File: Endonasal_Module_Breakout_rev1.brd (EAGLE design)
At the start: 80 x 100 mm, 43 parts, among them M0_LIMIT_XOR XOR-SOT353, M3_LIMIT_XOR XOR-SOT353

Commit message: All traces routed
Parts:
- removed M0_LEDG, M1_LEDG, M2_LEDG, M3_LEDG, M4_LEDG, M5_LEDG: (no value), Cannula_1_0:LED-0805
- removed R2, R3, R4, R5, R6: 220, Cannula_1_0:0603-RES
- added POWER_LEDG: (no value), Cannula_1_0:LED-0805
- moved C7 15.2 mm to (43.8, 56.5)
- moved R13 12.1 mm to (43.8, 60.1), turned to 90 degrees
- moved R1 11.4 mm to (5.08, 39.1), turned to 180 degrees
- moved C9 4.13 mm to (30.5, 60.6)
- moved M3_LIMIT_XOR 4.13 mm to (28.2, 60.7)
- moved C5 3.05 mm to (32.0, 36.6)
- moved R11 2.54 mm to (32.0, 33.0)
- moved R17 2.36 mm to (56.1, 35.4)
- moved R19 1.08 mm to (55.4, 18.1), turned to 180 degrees
- moved R18 0.34 mm to (56.0, 25.7), turned to 270 degrees
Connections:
- removed net N$1: M5_LEDG.A, R6.1
- removed net N$2: M4_LEDG.A, R5.1
- removed net N$3: M3_LEDG.A, R4.1
- removed net N$4: M2_LEDG.A, R3.1
- removed net N$5: M1_LEDG.A, R2.1
- net GND: now also POWER_LEDG.C; no longer M0_LEDG.C, M1_LEDG.C, M2_LEDG.C, M3_LEDG.C, M4_LEDG.C, M5_LEDG.C
- net M0_VHALL: now also R1.2
- net M2_VHALL: no longer R1.2, R2.2, R3.2
- net M3_VHALL: no longer R4.2
- net M4_VHALL: no longer R5.2
- net M5_HALL1: now also R19.2; no longer R19.1
- net M5_HALL2: now also R19.1; no longer R19.2
- net M5_VHALL: no longer R6.2
- net N$6: now also POWER_LEDG.A; no longer M0_LEDG.A
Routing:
- net M2A: track 5.08 -> 181.9 mm
- net M2B: track 5.08 -> 174.6 mm
- net M2C: track 5.08 -> 167.3 mm
- net M1A: track 7.18 -> 152.0 mm
- net M1B: track 7.18 -> 146.8 mm
- net M1C: track 7.18 -> 141.8 mm
- net M0A: track 5.08 -> 115.4 mm
- net M0B: track 5.08 -> 108.8 mm
- net M0C: track 5.08 -> 98.1 mm
- net 3.3V_IN: track 30.8 -> 111.8 mm
- net M0_VHALL: track 38.6 -> 84.5 mm
- net M3_VHALL: track 2.21 -> 46.9 mm
- net M4_VHALL: track 0.00 -> 43.2 mm
- net M3_HALL2: track 0.00 -> 40.2 mm
- net M3_HALL3: track 0.00 -> 38.4 mm
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
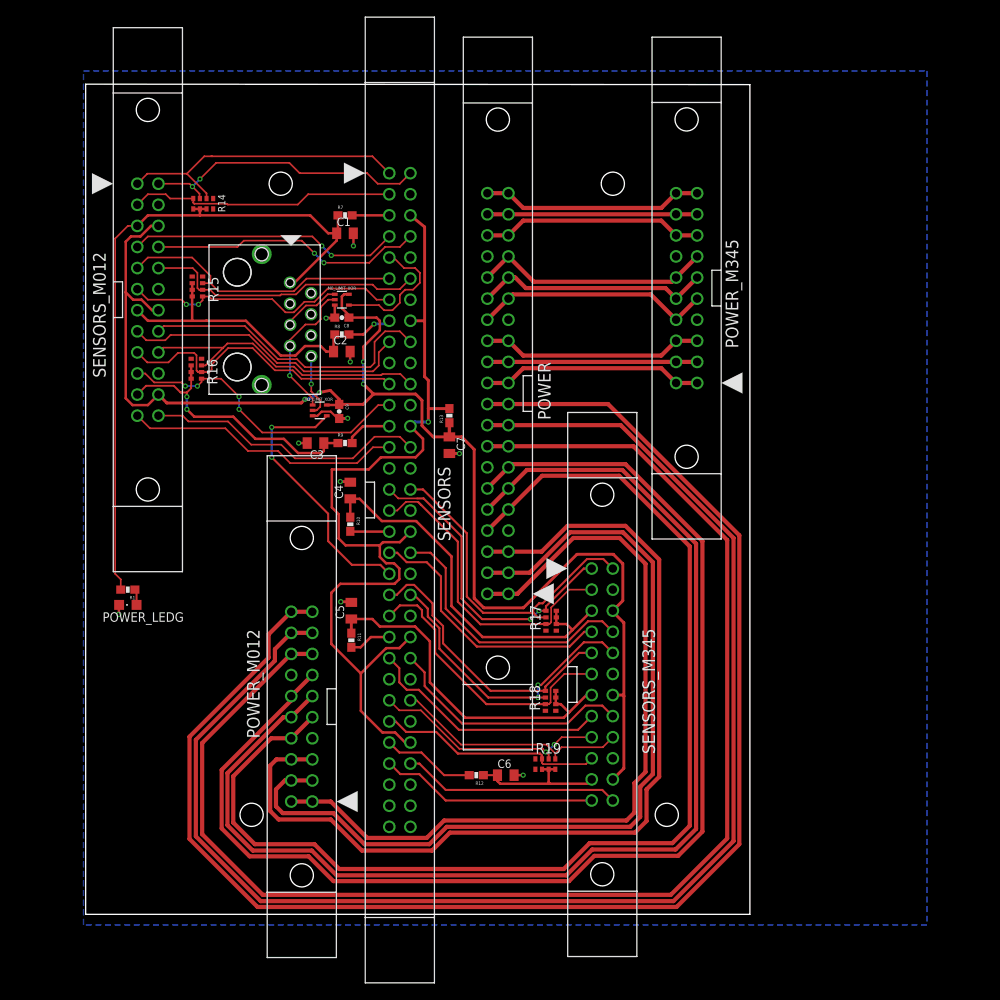
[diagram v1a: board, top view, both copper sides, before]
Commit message: Increased connector spacing
Increased spacing between connectors to be at least 5mm
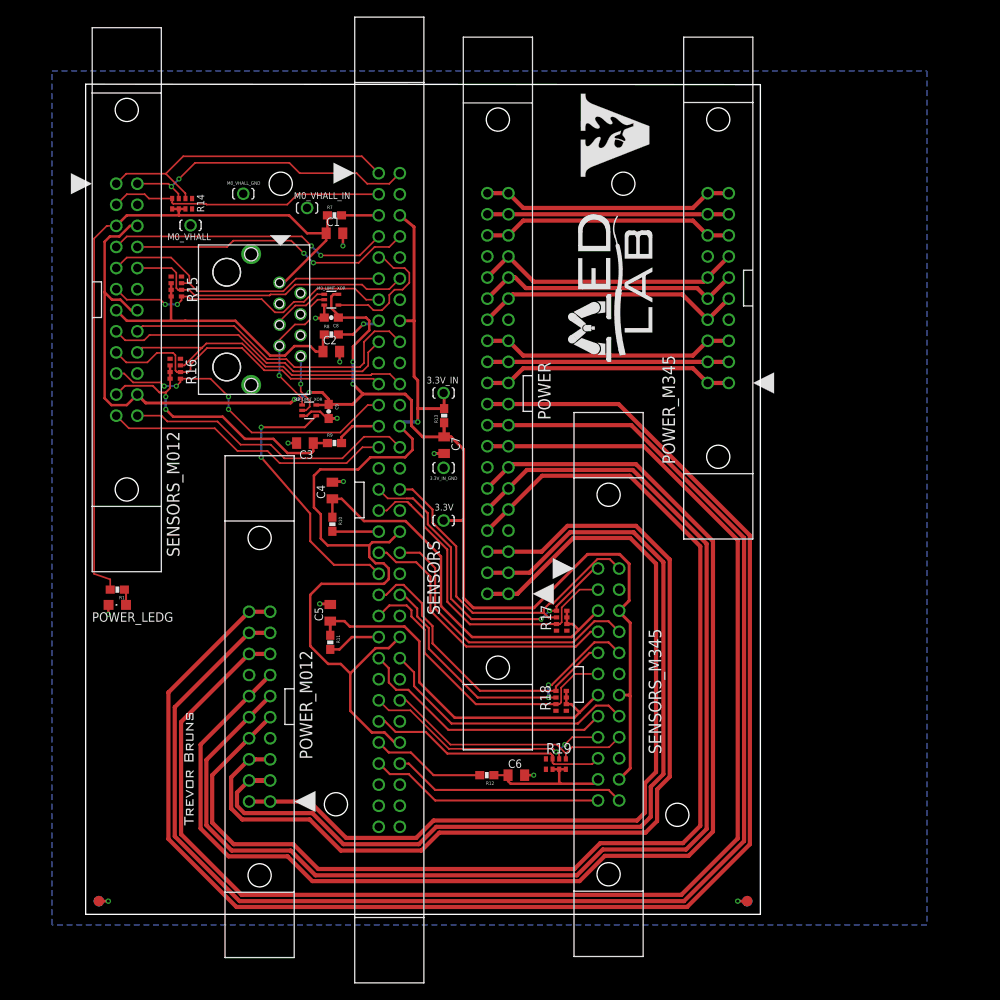
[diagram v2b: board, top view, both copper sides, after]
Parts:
- added 3.3V, 3.3V_IN, 3.3V_IN_GND, M0_VHALL, M0_VHALL_GND, M0_VHALL_IN: TEST-POINT_5021, Cannula_1_0:TEST-POINT_5021
- added TP1, TP2, TP3, TP4: TEST-POINT3X5, Cannula_1_0:PAD.03X.05
- added U$1: (no value), Cannula_1_0:LOGO_MEDLAB_3X2
- added U$2: (no value), Cannula_1_0:LOGO_V_OAK
- added U$3: (no value), Cannula_1_0:LOGO_TREVOR_SMALL
- added U$4: (no value), Cannula_1_0:LOGO_MEDLAB_0.7X0.4
- moved POWER_M012 5.08 mm to (21.0, 25.0)
- moved POWER_M345 3.81 mm to (76.2, 75.4)
- moved R11 2.55 mm to (29.5, 32.8)
- moved C5 2.55 mm to (29.5, 36.3)
- moved R14 2.54 mm to (11.6, 85.6)
- moved R16 2.54 mm to (10.8, 65.7)
- moved SENSORS_M012 2.54 mm to (4.95, 74.0)
- moved R15 2.54 mm to (10.9, 75.6)
- moved C4 2.16 mm to (29.7, 51.1)
- moved R10 2.16 mm to (29.7, 47.0)
- moved C6 1.27 mm to (51.9, 16.8)
- moved C9 1.27 mm to (29.3, 60.6)
- moved R12 1.27 mm to (48.3, 16.8)
- moved R18 1.27 mm to (57.3, 25.7)
- moved R19 1.27 mm to (56.6, 18.1)
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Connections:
- net 3.3V: now also 3.3V.P$1
- net 3.3V_IN: now also 3.3V_IN.P$1
- net GND: now also 3.3V_IN_GND.P$1, M0_VHALL_GND.P$1, TP1.P$1, TP2.P$1, TP3.P$1, TP4.P$1
- net M0_VHALL: now also M0_VHALL.P$1
- net M0_VHALL_IN: now also M0_VHALL_IN.P$1
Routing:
- net M0B: track 108.8 -> 117.1 mm
- net M0C: track 98.1 -> 105.7 mm
- net M0A: track 115.4 -> 122.1 mm
- net 3.3V_IN: track 111.8 -> 118.2 mm
- net 3.3V: track 167.8 -> 173.5 mm
- net M2B: track 174.6 -> 178.6 mm
- net M2A: track 181.9 -> 185.9 mm
- net M2C: track 167.3 -> 171.3 mm
- net M1A: track 152.0 -> 156.0 mm
- net M4C: track 28.9 -> 32.7 mm
- net M5C: track 26.7 -> 30.6 mm
- net M5B: track 25.3 -> 29.1 mm
- net M5A: track 26.7 -> 30.6 mm
- net M4B: track 28.4 -> 32.2 mm
- net M4A: track 28.9 -> 32.7 mm
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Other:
- board size 80 x 100 mm -> 81.3 x 100 mm

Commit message: Silkscreen
Set font sizes for passives
Renumbered components
Created net classes for POWER and MOTOR
Ran DRC and ERC
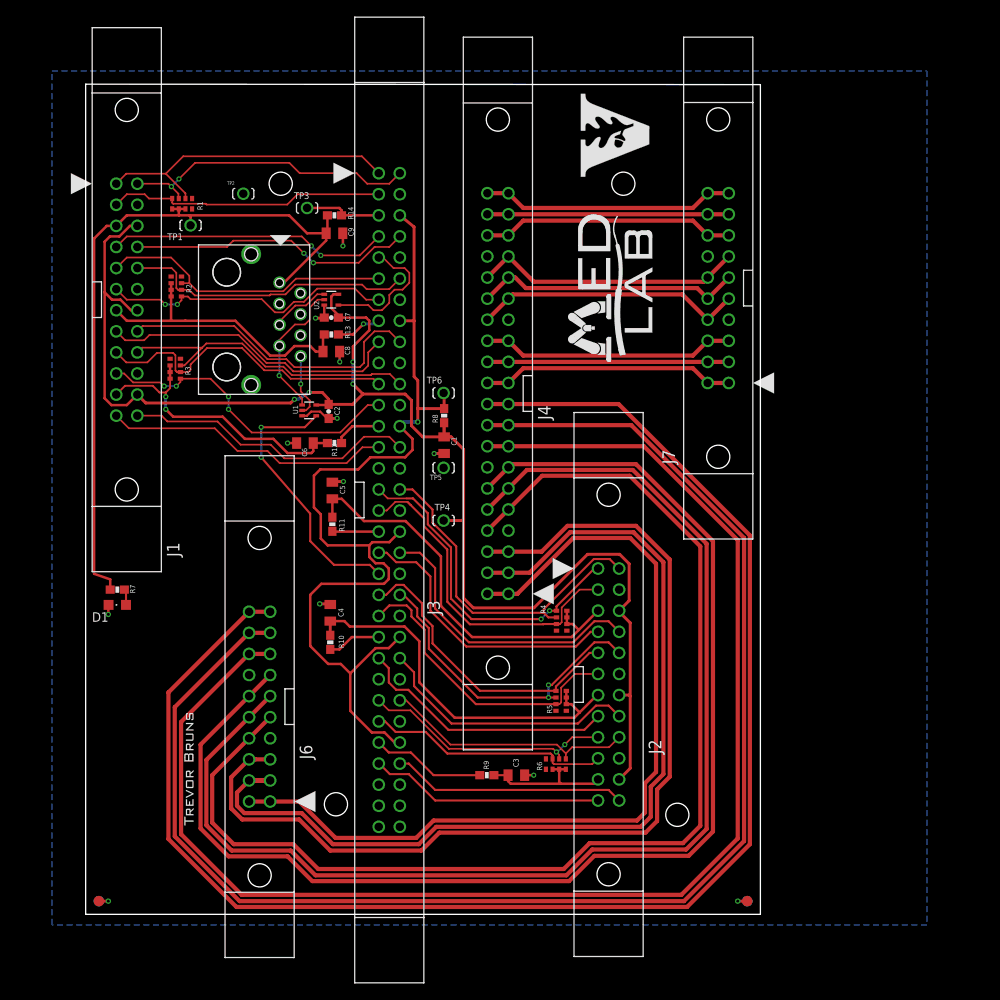
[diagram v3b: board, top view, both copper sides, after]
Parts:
- removed 3.3V, M0_VHALL, M0_VHALL_GND, M0_VHALL_IN: TEST-POINT_5021, Cannula_1_0:TEST-POINT_5021
- added TP10, TP7, TP8, TP9: TEST-POINT3X5, Cannula_1_0:PAD.03X.05
- C2, C7: value 10uF -> 0.1uF; device Cannula_1_0:C0805K -> SparkFun-Capacitors:0603-CAP
- C8, C9: value 0.1uF -> 10uF; device SparkFun-Capacitors:0603-CAP -> Cannula_1_0:C0805K
- D1: value (none) -> LEDG
- R1: value 220 -> 10K; device Cannula_1_0:0603-RES -> SparkFun-Passives:0603-ARV
- R14: value (none) -> 1; device SparkFun-Passives:0603-ARV -> Cannula_1_0:0603-RES
- R2, R3, R4, R5, R6: value (none) -> 10K
- R7: value 1 -> 220
- TP1, TP2, TP3, TP4: value TEST-POINT3X5 -> TEST-POINT_5021; device Cannula_1_0:PAD.03X.05 -> Cannula_1_0:TEST-POINT_5021
- U1: value XOR-SOT353 -> OR_M3
- U2: value XOR-SOT353 -> OR_M0
- moved TP1 105.5 mm to (12.6, 83.0)
- moved TP2 104.6 mm to (19.0, 86.8), flipped to the top
- moved TP3 87.2 mm to (26.7, 85.1)
- moved TP4 61.9 mm to (43.1, 47.4), flipped to the top
- moved R7 52.1 mm to (3.81, 39.1), turned to 180 degrees
- moved C3 47.4 mm to (51.9, 16.8), turned to 0 degrees
- moved C6 47.4 mm to (26.4, 56.8), turned to 180 degrees
- moved R1 47.1 mm to (11.6, 85.6), turned to 0 degrees
- moved R12 44.0 mm to (30.0, 56.8), turned to 0 degrees
- moved R9 44.0 mm to (48.3, 16.8), turned to 180 degrees
- moved C1 28.7 mm to (43.2, 56.5), turned to 270 degrees
- moved C9 21.5 mm to (30.0, 82.0), turned to 0 degrees
- moved C7 20.5 mm to (29.6, 71.9), turned to 180 degrees
- moved R14 18.4 mm to (30.0, 84.2)
- moved R13 16.7 mm to (29.6, 69.8), turned to 0 degrees
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- renumbered 3.3V_IN to TP6, 3.3V_IN_GND to TP5, LIMIT to J5, M0_LIMIT_XOR to U2, M3_LIMIT_XOR to U1, POWER to J4, POWER_LEDG to D1, POWER_M012 to J6, POWER_M345 to J7, R15 to R2, R16 to R3, R17 to R4, R18 to R5, R19 to R6, SENSORS to J3, SENSORS_M012 to J1, SENSORS_M345 to J2
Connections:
- net 3.3V: now also C1.1, C2.1, R8.1, TP4.P$1; no longer 3.3V.P$1, C8.1, C9.1, R13.1
- net 3.3V_IN: now also R8.2; no longer R13.2
- net GND: now also TP10.P$1, TP7.P$1, TP8.P$1, TP9.P$1; no longer M0_VHALL_GND.P$1, TP1.P$1, TP3.P$1, TP4.P$1
- net M0_HALL1: now also R1.6; no longer R14.6
- net M0_HALL2: now also R1.7; no longer R14.7
- net M0_HALL3: now also R1.8; no longer R14.8
- net M0_VHALL: now also C9.1, R1.1, R1.3, R7.2, TP1.P$1; no longer C1.1, M0_VHALL.P$1, R14.2, R14.3, R7.1
- net M0_VHALL_IN: now also R14.2, TP3.P$1; no longer M0_VHALL_IN.P$1, R7.2
- net M1_VHALL: now also C8.1, R13.1; no longer C2.1, R8.1
- net M1_VHALL_IN: now also R13.2; no longer R8.2
- net M2_VHALL: now also C6.1, R12.1; no longer C3.1, R9.1
- net M2_VHALL_IN: now also R12.2; no longer R9.2
- net M3_VHALL: now also C5.1, R11.1; no longer C4.1, R10.1
- net M3_VHALL_IN: now also R11.2; no longer R10.2
- net M4_VHALL: now also C4.1, R10.1; no longer C5.1, R11.1
- net M4_VHALL_IN: now also R10.2; no longer R11.2
- net M5_VHALL: now also C3.1, R9.1; no longer C6.1, R12.1
- net M5_VHALL_IN: now also R9.2; no longer R12.2
- net N$6: now also R7.1; no longer R1.1
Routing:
- net M0_VHALL_IN: track 4.48 -> 9.36 mm
- net M0_VHALL: track 86.9 -> 88.1 mm

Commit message: Layout finished (hopefully)
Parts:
- removed TP1, TP2, TP3, TP4, TP6: TEST-POINT_5021, Cannula_1_0:TEST-POINT_5021
- removed U$3: (no value), Cannula_1_0:LOGO_TREVOR_SMALL
- added 3.3V, 3.3V-IN, 5V, 5V-IN, GND: TEST-POINT_5021, Cannula_1_0:TEST-POINT_5021
- added U$5: (no value), Cannula_1_0:LOGO_ENDONASAL_BREAKOUT_1.0
- C2, C7: value 0.1uF -> 10uF; device SparkFun-Capacitors:0603-CAP -> Cannula_1_0:C0805K
- C3, C8: value 10uF -> 0.1uF; device Cannula_1_0:C0805K -> SparkFun-Capacitors:0603-CAP
- J1, J2: value CONN_RECT_2X12TH -> CONN_RECT_2X10TH; device Cannula_1_0:CONN_IDC_24_MALE_TH -> Cannula_1_0:CONN_IDC_20_MALE_TH
- J3: value CONN_RECT_2X32NOHOLES -> JACK_8P8C_RJ45_ETHERNET; device Cannula_1_0:CONN_IDC_64_MALE_TH_NOHOLES -> Cannula_1_0:ETHERNET_A104932
- J5: value JACK_8P8C_RJ45_ETHERNET -> CONN_RECT_2X32NOHOLES; device Cannula_1_0:ETHERNET_A104932 -> Cannula_1_0:CONN_IDC_64_MALE_TH_NOHOLES
- J6, J7: value CONN_RECT_2X10TH -> CONN_RECT_2X12TH; device Cannula_1_0:CONN_IDC_20_MALE_TH -> Cannula_1_0:CONN_IDC_24_MALE_TH
- R1, R2, R3, R4, R5, R6: value 10K -> 1; device SparkFun-Passives:0603-ARV -> Cannula_1_0:0603-RES
- R10, R11, R12, R13, R14, R9: value 1 -> 10K; device Cannula_1_0:0603-RES -> SparkFun-Passives:0603-ARV
- R7: value 220 -> 1
- R8: value 1 -> 220
- U1: value OR_M3 -> OR_M0
- U2: value OR_M0 -> OR_M3
- moved U$2 81.4 mm to (93.7, 18.9), turned to 0 degrees
- moved R1 80.3 mm to (84.2, 51.3), turned to 270 degrees
- moved TP10 78.1 mm to (1.59, 1.59), turned to 270 degrees
- moved TP7 78.1 mm to (1.59, 79.7), turned to 90 degrees
- moved TP8 78.1 mm to (1.59, 79.7), turned to 270 degrees
- moved TP9 78.1 mm to (1.59, 1.59), turned to 90 degrees
- moved J7 75.0 mm to (27.7, 18.3), turned to 180 degrees
- moved J6 73.8 mm to (74.0, 76.3), turned to 180 degrees
- moved R9 64.7 mm to (85.6, 69.7), turned to 270 degrees
- moved R2 63.6 mm to (69.8, 51.7), turned to 270 degrees
- moved R14 60.7 mm to (18.1, 24.6), turned to 90 degrees
- moved R10 59.5 mm to (75.6, 70.4), turned to 0 degrees
- moved U$4 58.8 mm to (74.1, 18.0), turned to 0 degrees
- moved R7 56.3 mm to (60.1, 38.1), turned to 0 degrees
- moved D1 52.3 mm to (37.3, 77.5), turned to 0 degrees
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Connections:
- net 3.3V: now also 3.3V.P$1, C3.1, C8.1, C9.1, J6.P$14, J6.P$22, J6.P$6, J7.P$14, J7.P$22, J7.P$6, R7.1; no longer C1.1, C2.1, C7.1, J1.P$14, J1.P$22, J1.P$6, J2.P$14, J2.P$22, J2.P$6, R8.1, TP4.P$1
- net 3.3V_IN: now also 3.3V-IN.P$1, J5.P$16, J5.P$26, J5.P$36, J5.P$46, J5.P$56, J5.P$6, R7.2; no longer J3.P$16, J3.P$26, J3.P$36, J3.P$46, J3.P$56, J3.P$6, R8.2, TP6.P$1
- net GND: now also GND.P$1, J3.SHIELD1, J3.SHIELD2, J5.P$10, J5.P$14, J5.P$20, J5.P$24, J5.P$30, J5.P$34, J5.P$4, J5.P$40, J5.P$44, J5.P$50, J5.P$54, J5.P$60, J6.P$12, J6.P$20, J6.P$4, J7.P$12, J7.P$20, J7.P$4; no longer J1.P$12, J1.P$20, J1.P$4, J2.P$12, J2.P$20, J2.P$4, J3.P$10, J3.P$14, J3.P$20, J3.P$24, J3.P$30, J3.P$34, J3.P$4, J3.P$40, J3.P$44, J3.P$50, J3.P$54, J3.P$60, J5.SHIELD1, J5.SHIELD2, TP2.P$1
- net LIMIT1: now also J3.P$5, U1.1; no longer J5.P$5, U2.1
- net LIMIT2: now also J3.P$7, U1.2, U2.1; no longer J5.P$7, U1.1, U2.2
- net LIMIT3: now also J3.P$8, U2.2; no longer J5.P$8, U1.2
- net M0A: now also J1.P$5, J1.P$6; no longer J6.P$5, J6.P$6
- net M0B: now also J1.P$3, J1.P$4; no longer J6.P$3, J6.P$4
- net M0C: now also J1.P$1, J1.P$2; no longer J6.P$1, J6.P$2
- net M0_ENC_A: now also J5.P$7, J6.P$7; no longer J1.P$7, J3.P$7
- net M0_ENC_B: now also J5.P$8, J6.P$8; no longer J1.P$8, J3.P$8
- net M0_HALL1: now also J5.P$1, J6.P$1, R9.6; no longer J1.P$1, J3.P$1, R1.6
- net M0_HALL2: now also J5.P$2, J6.P$2, R9.7; no longer J1.P$2, J3.P$2, R1.7
- net M0_HALL3: now also J5.P$3, J6.P$3, R9.8; no longer J1.P$3, J3.P$3, R1.8
- net M0_LIMIT: now also J5.P$9, U1.4; no longer J3.P$9, U2.4
- net M0_VHALL: now also 5V.P$1, C1.1, J3.P$1, J6.P$5, R8.2, R9.1, R9.2, R9.3; no longer C9.1, J1.P$5, J5.P$1, R1.2, R1.3, R14.1, R7.2, TP1.P$1
- net M0_VHALL_IN: now also 5V-IN.P$1, J5.P$5, R1.2; no longer J3.P$5, R14.2, TP3.P$1
- net M1A: now also J1.P$12, J1.P$13; no longer J6.P$12, J6.P$13
- net M1B: now also J1.P$10, J1.P$11; no longer J6.P$10, J6.P$11
- net M1C: now also J1.P$8, J1.P$9; no longer J6.P$8, J6.P$9
- net M1_ENC_A: now also J5.P$17, J6.P$15; no longer J1.P$15, J3.P$17
- net M1_ENC_B: now also J5.P$18, J6.P$16; no longer J1.P$16, J3.P$18
- net M1_HALL1: now also J5.P$11, J6.P$9, R10.3; no longer J1.P$9, J3.P$11, R2.3
- net M1_HALL2: now also J5.P$12, J6.P$10, R10.2; no longer J1.P$10, J3.P$12, R2.2
- net M1_HALL3: now also J5.P$13, J6.P$11, R10.1; no longer J1.P$11, J3.P$13, R2.1
- net M1_LIMIT: now also J5.P$19; no longer J3.P$19
- net M1_VHALL: now also C2.1, J6.P$13, R10.6, R10.7, R10.8, R2.1; no longer C8.1, J1.P$13, R13.1, R2.6, R2.7, R2.8
- net M1_VHALL_IN: now also J5.P$15, R2.2; no longer J3.P$15, R13.2
- net M2A: now also J1.P$19, J1.P$20; no longer J6.P$19, J6.P$20
- net M2B: now also J1.P$17, J1.P$18; no longer J6.P$17, J6.P$18
- net M2C: now also J1.P$15, J1.P$16; no longer J6.P$15, J6.P$16
- net M2_ENC_A: now also J5.P$27, J6.P$23; no longer J1.P$23, J3.P$27
- net M2_ENC_B: now also J5.P$28, J6.P$24; no longer J1.P$24, J3.P$28
- net M2_HALL1: now also J5.P$21, J6.P$17, R11.2; no longer J1.P$17, J3.P$21, R3.2
- net M2_HALL2: now also J5.P$22, J6.P$18, R11.3; no longer J1.P$18, J3.P$22, R3.3
- net M2_HALL3: now also J5.P$23, J6.P$19, R11.1; no longer J1.P$19, J3.P$23, R3.1
- net M2_LIMIT: now also J5.P$29; no longer J3.P$29
- net M2_VHALL: now also C4.1, J6.P$21, R11.6, R11.7, R11.8, R3.1; no longer C6.1, J1.P$21, R12.1, R3.6, R3.7, R3.8
- net M2_VHALL_IN: now also J5.P$25, R3.2; no longer J3.P$25, R12.2
- net M3A: now also J2.P$5, J2.P$6; no longer J7.P$5, J7.P$6
- net M3B: now also J2.P$3, J2.P$4; no longer J7.P$3, J7.P$4
- net M3C: now also J2.P$1, J2.P$2; no longer J7.P$1, J7.P$2
- net M3_ENC_A: now also J5.P$37, J7.P$7; no longer J2.P$7, J3.P$37
- net M3_ENC_B: now also J5.P$38, J7.P$8; no longer J2.P$8, J3.P$38
- net M3_HALL1: now also J5.P$31, J7.P$1, R12.1; no longer J2.P$1, J3.P$31, R4.1
- net M3_HALL2: now also J5.P$32, J7.P$2, R12.2; no longer J2.P$2, J3.P$32, R4.2
- net M3_HALL3: now also J5.P$33, J7.P$3, R12.3; no longer J2.P$3, J3.P$33, R4.3
- net M3_LIMIT: now also J5.P$39, U2.4; no longer J3.P$39, U1.4
- net M3_VHALL: now also J7.P$5, R12.6, R12.7, R12.8, R4.1; no longer J2.P$5, R11.1, R4.6, R4.7, R4.8
- net M3_VHALL_IN: now also J5.P$35, R4.2; no longer J3.P$35, R11.2
- net M4A: now also J2.P$12, J2.P$13; no longer J7.P$12, J7.P$13
- net M4B: now also J2.P$10, J2.P$11; no longer J7.P$10, J7.P$11
- net M4C: now also J2.P$8, J2.P$9; no longer J7.P$8, J7.P$9
- net M4_ENC_A: now also J5.P$47, J7.P$15; no longer J2.P$15, J3.P$47
- net M4_ENC_B: now also J5.P$48, J7.P$16; no longer J2.P$16, J3.P$48
- net M4_HALL1: now also J5.P$41, J7.P$9, R13.1; no longer J2.P$9, J3.P$41, R5.1
- net M4_HALL2: now also J5.P$42, J7.P$10, R13.2; no longer J2.P$10, J3.P$42, R5.2
- net M4_HALL3: now also J5.P$43, J7.P$11, R13.3; no longer J2.P$11, J3.P$43, R5.3
- net M4_LIMIT: now also J5.P$49; no longer J3.P$49
- net M4_VHALL: now also C6.1, J7.P$13, R13.6, R13.7, R13.8, R5.1; no longer C4.1, J2.P$13, R10.1, R5.6, R5.7, R5.8
- net M4_VHALL_IN: now also J5.P$45, R5.2; no longer J3.P$45, R10.2
- net M5A: now also J2.P$19, J2.P$20; no longer J7.P$19, J7.P$20
- net M5B: now also J2.P$17, J2.P$18; no longer J7.P$17, J7.P$18
- net M5C: now also J2.P$15, J2.P$16; no longer J7.P$15, J7.P$16
- net M5_ENC_A: now also J5.P$57, J7.P$23; no longer J2.P$23, J3.P$57
- net M5_ENC_B: now also J5.P$58, J7.P$24; no longer J2.P$24, J3.P$58
- net M5_HALL1: now also J5.P$51, J7.P$17, R14.2; no longer J2.P$17, J3.P$51, R6.2
- net M5_HALL2: now also J5.P$52, J7.P$18, R14.1; no longer J2.P$18, J3.P$52, R6.1
- net M5_HALL3: now also J5.P$53, J7.P$19, R14.3; no longer J2.P$19, J3.P$53, R6.3
- net M5_LIMIT: now also J5.P$59; no longer J3.P$59
- net M5_VHALL: now also C7.1, J7.P$21, R14.6, R14.7, R14.8, R6.1; no longer C3.1, J2.P$21, R6.6, R6.7, R6.8, R9.1
- net M5_VHALL_IN: now also J5.P$55, R6.2; no longer J3.P$55, R9.2
- net N$190: now also J5.P$62; no longer J3.P$62
- net N$191: now also J5.P$63; no longer J3.P$63
- net N$192: now also J5.P$64; no longer J3.P$64
- net N$6: now also R8.1; no longer R7.1
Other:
- board size 81.3 x 100 mm -> 100 x 81.3 mm
- board text added: "GND"
- board text added: "Motor"
- board text added: "Motor- M0/M1/M2"
- board text added: "Motor- M3/M4/M5"
- board text added: "Sensor"
- board text added: "Sensor- M0/M1/M2"
- board text added: "Sensor- M3/M4/M5"
